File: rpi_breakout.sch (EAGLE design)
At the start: 20 parts

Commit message: New README. Some labeling tweaks on the board.
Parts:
- LED1: value CONN -> CONNECTED
- LED2: value POWER -> IO-POWER
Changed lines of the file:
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@@
 <grid distance="0.1" unitdist="inch" unit="inch" style="lines" multiple="1" display="no" altdistance="0.01" altunitdist="inch" altunit="inch"/>
 <layers>
-<layer number="1" name="Top" color="4" fill="1" visible="yes" active="no"/>
-<layer number="16" name="Bottom" color="1" fill="1" visible="yes" active="no"/>
-<layer number="17" name="Pads" color="2" fill="1" visible="yes" active="no"/>
-<layer number="18" name="Vias" color="2" fill="1" visible="yes" active="no"/>
-<layer number="19" name="Unrouted" color="6" fill="1" visible="yes" active="no"/>
-<layer number="20" name="Dimension" color="15" fill="1" visible="yes" active="no"/>
-<layer number="21" name="tPlace" color="7" fill="1" visible="yes" active="no"/>
-<layer number="22" name="bPlace" color="7" fill="1" visible="yes" active="no"/>
-<layer number="23" name="tOrigins" color="15" fill="1" visible="yes" active="no"/>
-<layer number="24" name="bOrigins" color="15" fill="1" visible="yes" active="no"/>
-<layer number="25" name="tNames" color="7" fill="1" visible="yes" active="no"/>
-<layer number="26" name="bNames" color="7" fill="1" visible="yes" active="no"/>
-<layer number="27" name="tValues" color="7" fill="1" visible="yes" active="no"/>
-<layer number="28" name="bValues" color="7" fill="1" visible="yes" active="no"/>
+<layer number="1" name="Top" color="4" fill="1" visible="no" active="no"/>
+<layer number="16" name="Bottom" color="1" fill="1" visible="no" active="no"/>
+<layer number="17" name="Pads" color="2" fill="1" visible="no" active="no"/>
+<layer number="18" name="Vias" color="2" fill="1" visible="no" active="no"/>
+<layer number="19" name="Unrouted" color="6" fill="1" visible="no" active="no"/>
+<layer number="20" name="Dimension" color="15" fill="1" visible="no" active="no"/>
+<layer number="21" name="tPlace" color="7" fill="1" visible="no" active="no"/>
+<layer number="22" name="bPlace" color="7" fill="1" visible="no" active="no"/>
+<layer number="23" name="tOrigins" color="15" fill="1" visible="no" active="no"/>
+<layer number="24" name="bOrigins" color="15" fill="1" visible="no" active="no"/>
+<layer number="25" name="tNames" color="7" fill="1" visible="no" active="no"/>
+<layer number="26" name="bNames" color="7" fill="1" visible="no" active="no"/>
+<layer number="27" name="tValues" color="7" fill="1" visible="no" active="no"/>
+<layer number="28" name="bValues" color="7" fill="1" visible="no" active="no"/>
 <layer number="29" name="tStop" color="7" fill="3" visible="no" active="no"/>
 <layer number="30" name="bStop" color="7" fill="6" visible="no" active="no"/>
@@
 <layer number="35" name="tGlue" color="7" fill="4" visible="no" active="no"/>
 <layer number="36" name="bGlue" color="7" fill="5" visible="no" active="no"/>
-<layer number="37" name="tTest" color="7" fill="1" visible="yes" active="no"/>
-<layer number="38" name="bTest" color="7" fill="1" visible="yes" active="no"/>
+<layer number="37" name="tTest" color="7" fill="1" visible="no" active="no"/>
+<layer number="38" name="bTest" color="7" fill="1" visible="no" active="no"/>
 <layer number="39" name="tKeepout" color="4" fill="11" visible="no" active="no"/>
 <layer number="40" name="bKeepout" color="1" fill="11" visible="no" active="no"/>
@@
 <layer number="44" name="Drills" color="7" fill="1" visible="no" active="no"/>
 <layer number="45" name="Holes" color="7" fill="1" visible="no" active="no"/>
-<layer number="46" name="Milling" color="3" fill="1" visible="yes" active="no"/>
-<layer number="47" name="Measures" color="7" fill="1" visible="yes" active="no"/>
-<layer number="48" name="Document" color="7" fill="1" visible="yes" active="no"/>
-<layer number="49" name="Reference" color="7" fill="1" visible="yes" active="no"/>
-<layer number="50" name="dxf" color="7" fill="1" visible="yes" active="no"/>
-<layer number="51" name="tDocu" color="7" fill="1" visible="yes" active="no"/>
-<layer number="52" name="bDocu" color="7" fill="1" visible="yes" active="no"/>
-<layer number="53" name="tGND_GNDA" color="7" fill="9" visible="yes" active="no"/>
-<layer number="54" name="bGND_GNDA" color="1" fill="9" visible="yes" active="no"/>
-<layer number="56" name="wert" color="7" fill="1" visible="yes" active="no"/>
+<layer number="46" name="Milling" color="3" fill="1" visible="no" active="no"/>
+<layer number="47" name="Measures" color="7" fill="1" visible="no" active="no"/>
+<layer number="48" name="Document" color="7" fill="1" visible="no" active="no"/>
+<layer number="49" name="Reference" color="7" fill="1" visible="no" active="no"/>
+<layer number="50" name="dxf" color="7" fill="1" visible="no" active="no"/>
+<layer number="51" name="tDocu" color="7" fill="1" visible="no" active="no"/>
+<layer number="52" name="bDocu" color="7" fill="1" visible="no" active="no"/>
+<layer number="53" name="tGND_GNDA" color="7" fill="9" visible="no" active="no"/>
+<layer number="54" name="bGND_GNDA" color="1" fill="9" visible="no" active="no"/>
+<layer number="56" name="wert" color="7" fill="1" visible="no" active="no"/>
 <layer number="91" name="Nets" color="2" fill="1" visible="yes" active="yes"/>
 <layer number="92" name="Busses" color="1" fill="1" visible="yes" active="yes"/>
@@
 <part name="GND5" library="SparkFun" deviceset="GND" device=""/>
 <part name="JP5" library="SparkFun" deviceset="M03" device="PTH" value="VTG-SEL"/>
-<part name="LED1" library="adafruit" deviceset="LED" device="CHIPLED_0805" value="CONN"/>
-<part name="LED2" library="adafruit" deviceset="LED" device="CHIPLED_0805" value="POWER"/>
+<part name="LED1" library="adafruit" deviceset="LED" device="CHIPLED_0805" value="CONNECTED"/>
+<part name="LED2" library="adafruit" deviceset="LED" device="CHIPLED_0805" value="IO-POWER"/>
 <part name="R3" library="SparkFun" deviceset="RESISTOR" device="0805-RES" value="330"/>
 <part name="GND6" library="SparkFun" deviceset="GND" device=""/>

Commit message: Split special-pin header into 2x6.
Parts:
- added JP8: (no value), adafruit:PINHD-1X1CB
- JP3: value COMM -> (none); device SparkFun:M12LOCK -> SparkFun:M06FEMALE_LOCK
- JP4: value IO-PWR-EXT -> (none); device SparkFun:M02PTH -> SparkFun:M06FEMALE_LOCK
- JP5: value VTG-SEL -> IO-PWR-EXT; device SparkFun:M03PTH -> SparkFun:M02PTH
- JP6: value (none) -> VTG-SEL; device adafruit:PINHD-1X1CB -> SparkFun:M03PTH
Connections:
- net N$3 renamed LED3_A
- net N$5 renamed LED4_A
- removed net N$4: JP6.1, R3.1
- removed net N$6: JP7.1, R4.1
- new net LED3_JP: JP7.1, R3.1
- new net LED4_JP: JP8.1, R4.1
- net /SPI_CEV0: now also JP4.1; no longer JP3.7
- net 3.3V: now also JP6.1; no longer JP5.1
- net 5V: now also JP6.3; no longer JP5.3
- net GND: now also JP5.2; no longer JP4.2
- net RXDV: now also JP4.6; no longer JP3.12
- net SPI_MISOV: now also JP4.2; no longer JP3.8
- net SPI_MOSIV: now also JP4.3; no longer JP3.9
- net SPI_SCLKV: now also JP4.4; no longer JP3.10
- net TXDV: now also JP4.5; no longer JP3.11
- net VCC: now also JP5.1, JP6.2; no longer JP4.1, JP5.2
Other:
- moved on the sheet: JP7

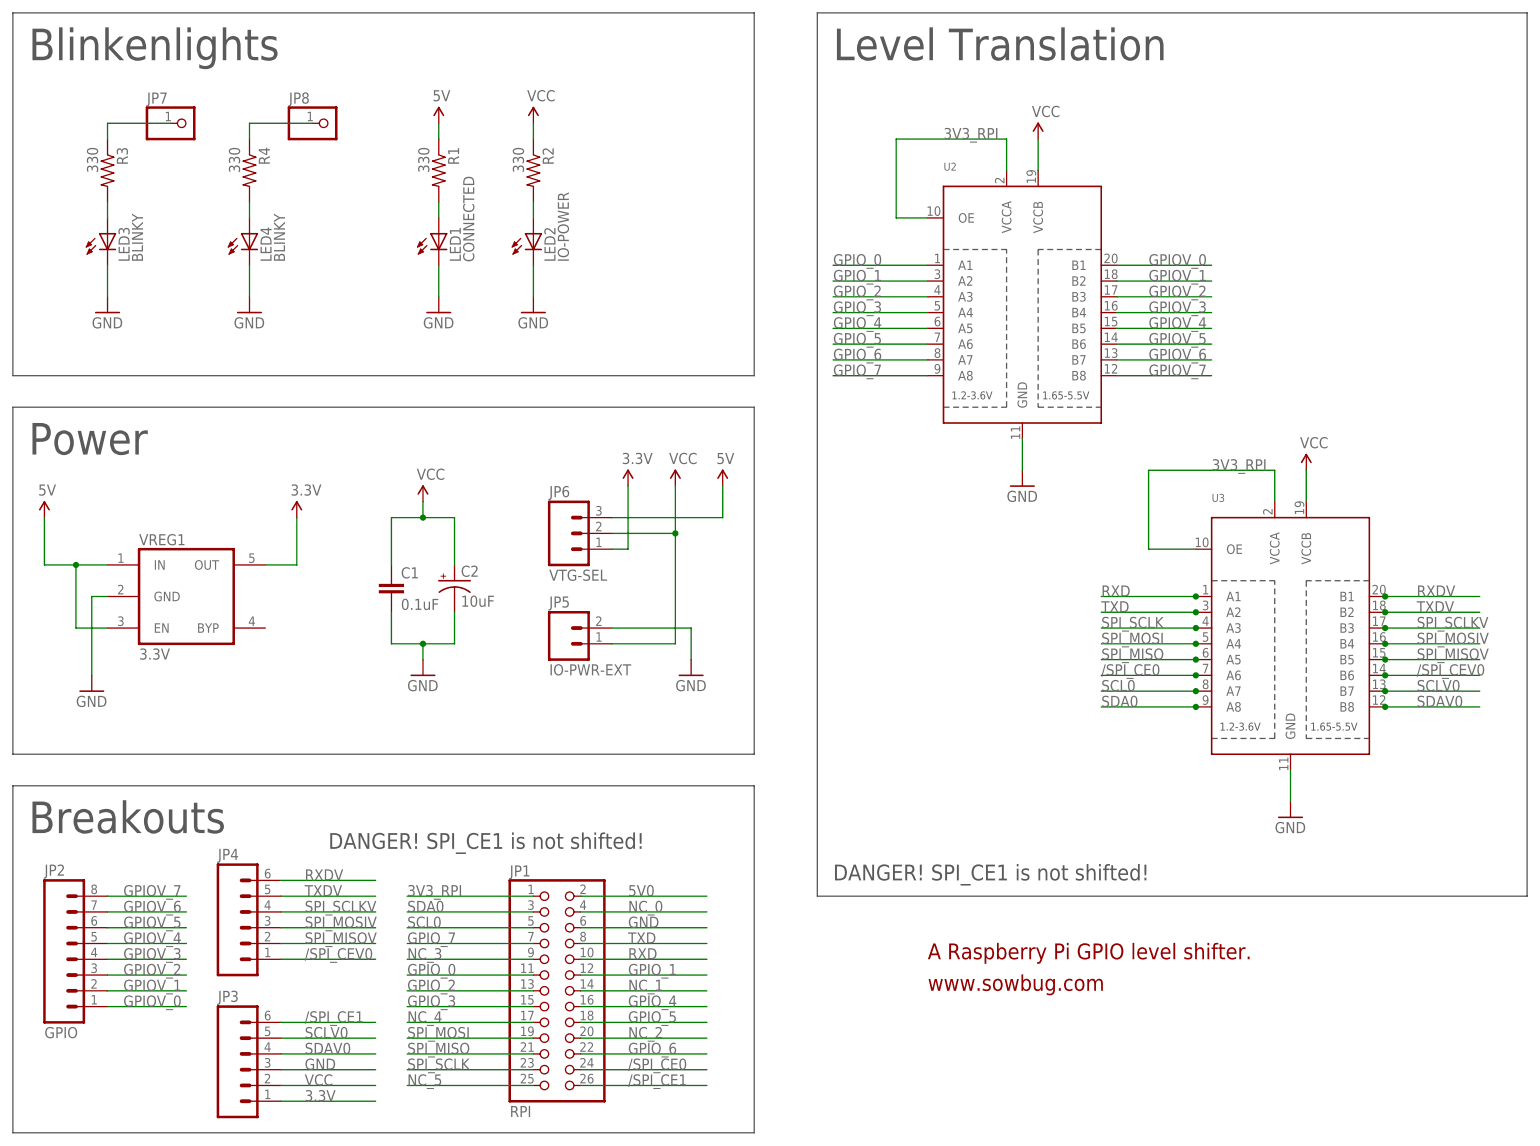
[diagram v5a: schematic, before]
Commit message: Smaller board footprint again; Merged from canton7's nice layout
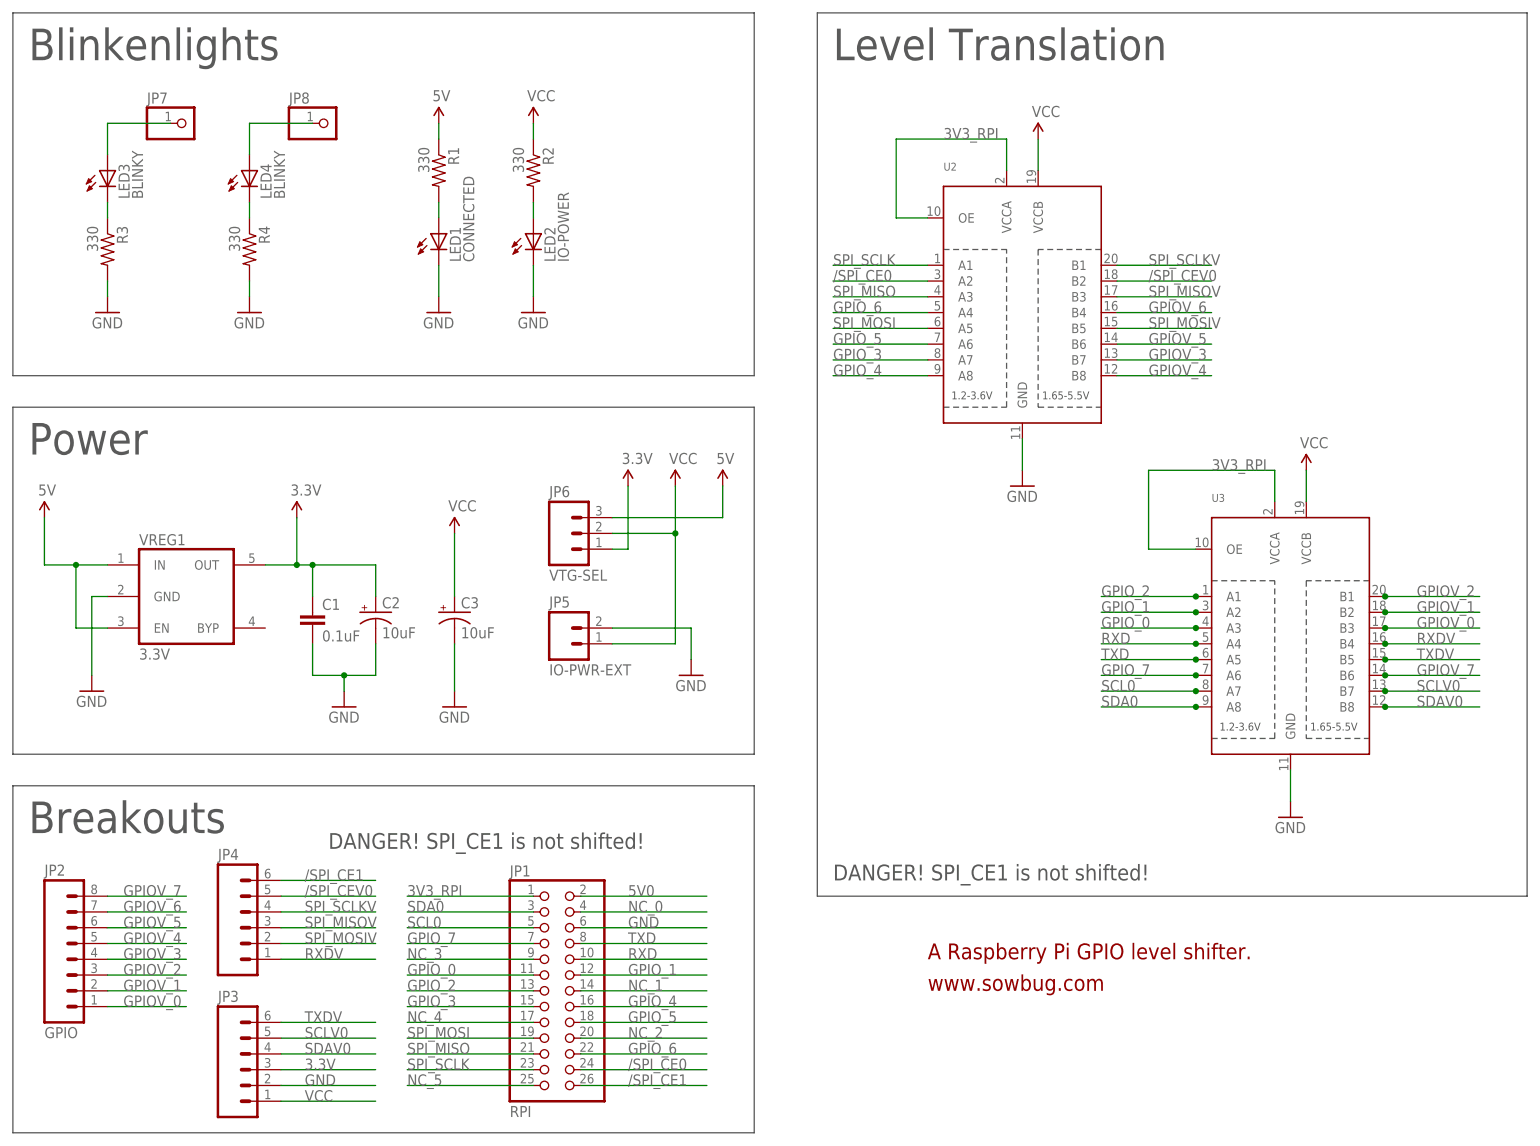
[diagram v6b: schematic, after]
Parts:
- added C3: 10uF, SparkFun:CAP_POL1206
- U2, U3: device adafruit:TXB0108PWR -> rpi_breakout:TXB0108PWR
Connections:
- removed net LED3_A: LED3.A, R3.2
- removed net LED4_A: LED4.A, R4.2
- new net N$3: LED3.C, R3.1
- new net N$4: LED4.C, R4.1
- net /SPI_CE0: now also U2.A2; no longer U3.A6
- net /SPI_CE1: now also JP4.6; no longer JP3.6
- net /SPI_CEV0: now also JP4.5, U2.B2; no longer JP4.1, U3.B6
- net 3.3V: now also C1.1, C2.+, JP3.3; no longer JP3.1
- net GND: now also C3.-, JP3.2, R3.2, R4.2; no longer JP3.3, LED3.C, LED4.C
- net GPIOV_0: now also U3.B3; no longer U2.B1
- net GPIOV_1: now also U3.B2; no longer U2.B2
- net GPIOV_2: now also U3.B1; no longer U2.B3
- net GPIOV_3: now also U2.B7; no longer U2.B4
- net GPIOV_4: now also U2.B8; no longer U2.B5
- net GPIOV_6: now also U2.B4; no longer U2.B7
- net GPIOV_7: now also U3.B6; no longer U2.B8
- net GPIO_0: now also U3.A3; no longer U2.A1
- net GPIO_1: now also U3.A2; no longer U2.A2
- net GPIO_2: now also U3.A1; no longer U2.A3
- net GPIO_3: now also U2.A7; no longer U2.A4
- net GPIO_4: now also U2.A8; no longer U2.A5
- net GPIO_6: now also U2.A4; no longer U2.A7
- net GPIO_7: now also U3.A6; no longer U2.A8
- net LED3_JP: now also LED3.A; no longer R3.1
- net LED4_JP: now also LED4.A; no longer R4.1
- net RXD: now also U3.A4; no longer U3.A1
- net RXDV: now also JP4.1, U3.B4; no longer JP4.6, U3.B1
- net SPI_MISO: now also U2.A3; no longer U3.A5
- net SPI_MISOV: now also JP4.3, U2.B3; no longer JP4.2, U3.B5
- net SPI_MOSI: now also U2.A5; no longer U3.A4
- net SPI_MOSIV: now also JP4.2, U2.B5; no longer JP4.3, U3.B4
- net SPI_SCLK: now also U2.A1; no longer U3.A3
- net SPI_SCLKV: now also U2.B1; no longer U3.B3
- net TXD: now also U3.A5; no longer U3.A2
- net TXDV: now also JP3.6, U3.B5; no longer JP4.5, U3.B2
- net VCC: now also C3.+, JP3.1; no longer C1.1, C2.+, JP3.2
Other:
- moved on the sheet: C1, C2, LED3, LED4, R3, R4

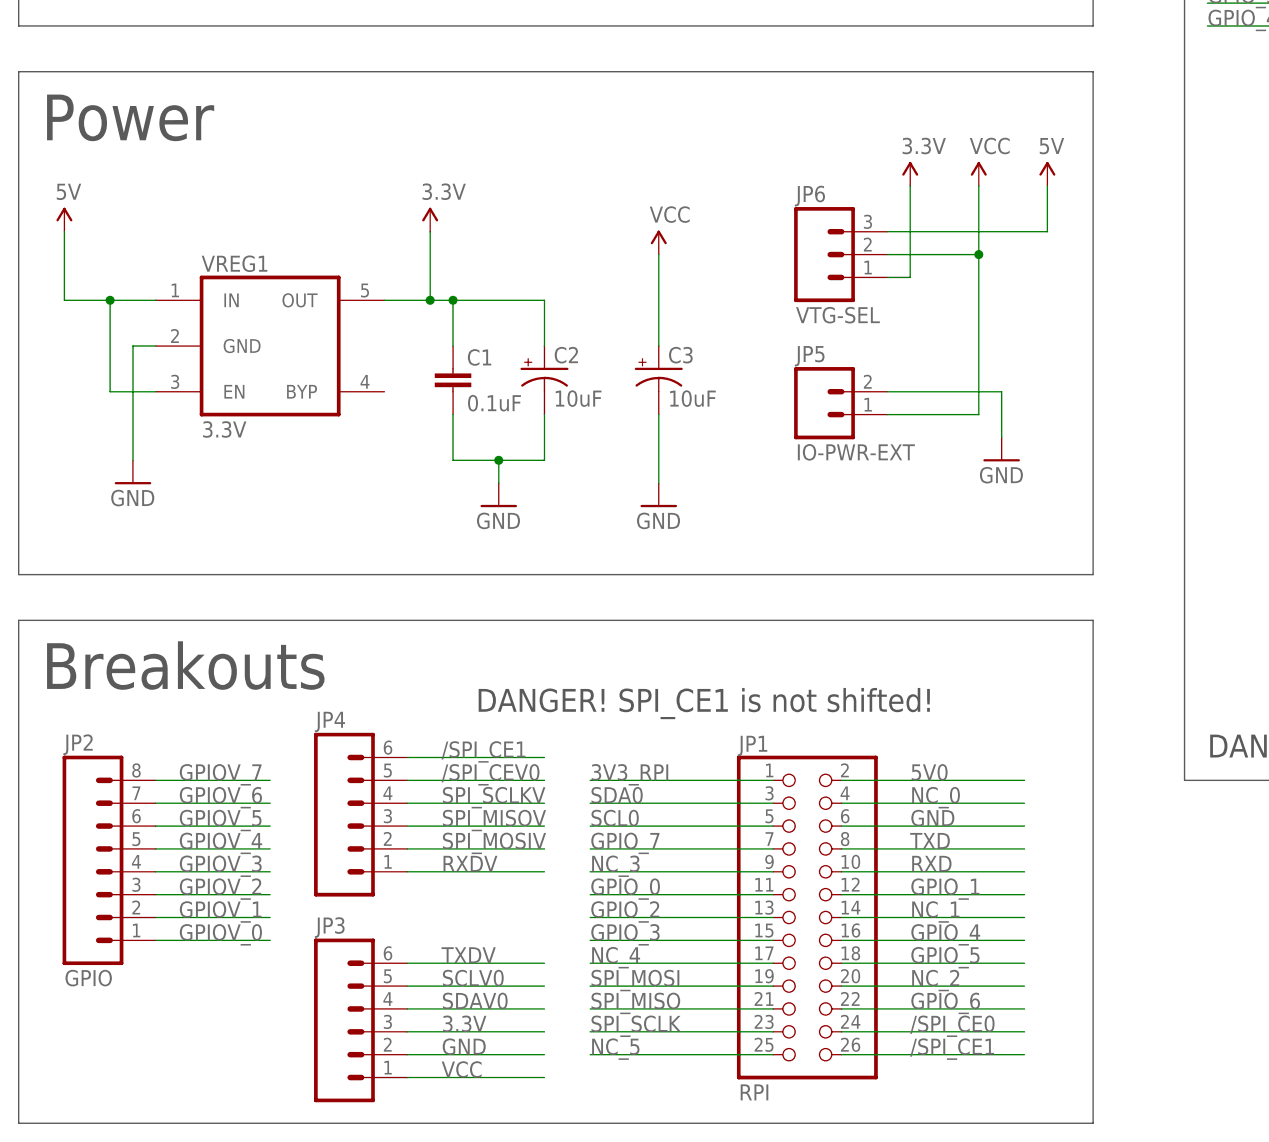
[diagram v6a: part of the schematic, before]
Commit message: Added solder jumper, RTC and diode protection, shortened traces (26.5 total)
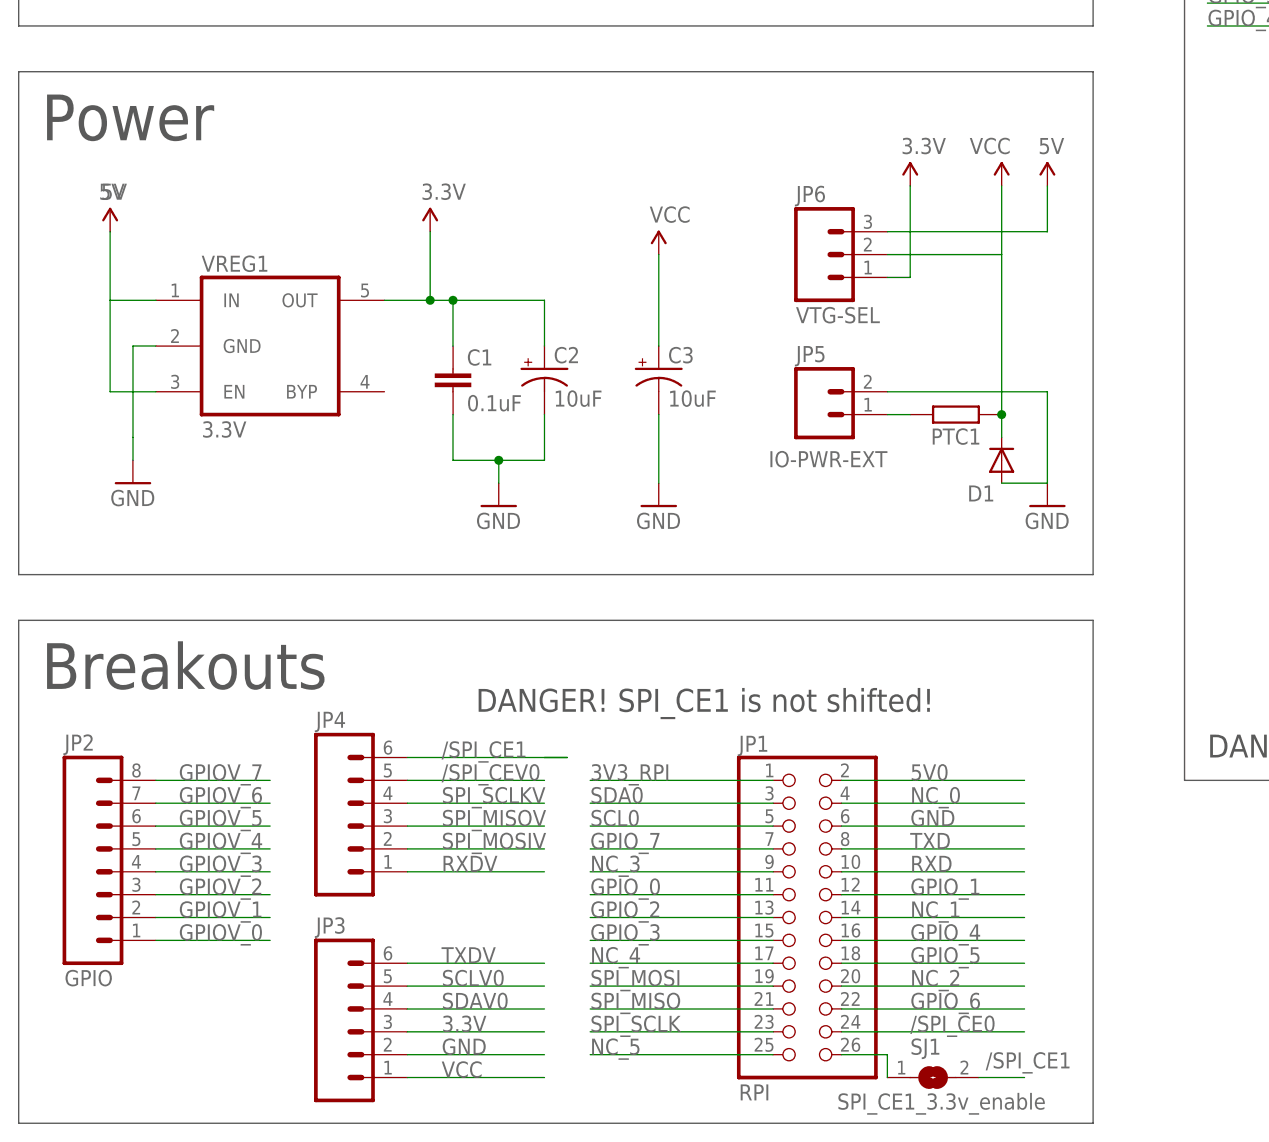
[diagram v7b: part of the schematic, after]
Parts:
- added D1: (no value), SparkFun-DiscreteSemi:DIODESOD
- added PTC1: (no value), rcl:R-EU_R1206
- added SJ1: SPI_CE1_3.3v_enable, jumper:SJ
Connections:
- new net N$5: JP1.26, SJ1.1
- new net N$6: JP5.1, PTC1.1
- net /SPI_CE1: now also SJ1.2; no longer JP1.26
- net GND: now also D1.A
- net VCC: now also D1.C, PTC1.2; no longer JP5.1
